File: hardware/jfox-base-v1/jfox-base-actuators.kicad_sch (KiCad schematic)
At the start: 3 parts, among them J80 ACT A, J81 ACT B, J82 ACT C

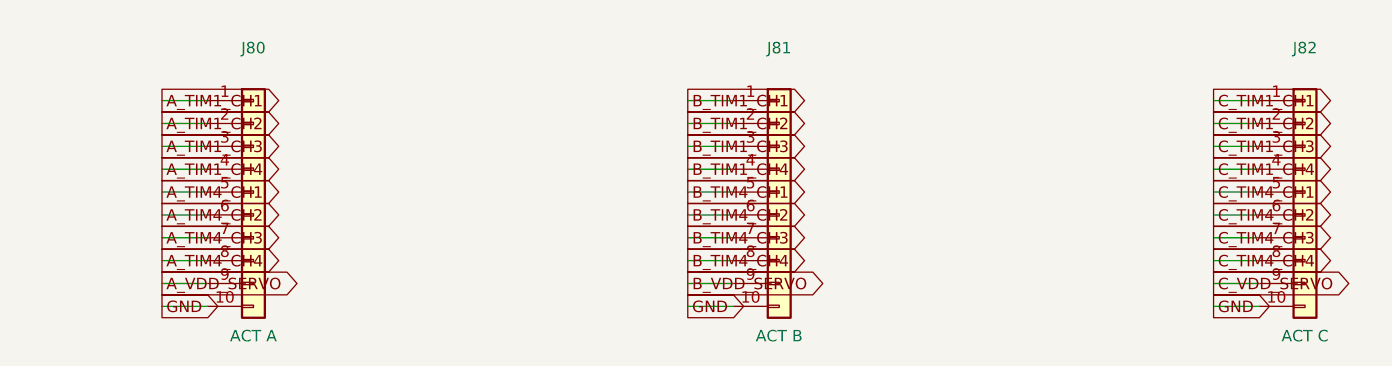
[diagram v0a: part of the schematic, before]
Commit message: LTC4417 lands on the backplane, replacing the diode OR
It left the FCU when the power tree moved and never arrived here - the
backplane has been ORing its two airframe feeds with a pair of Schottkys,
which works and throws away the two things the part was chosen for:

  * Priority. A diode OR takes whichever feed is momentarily higher, so two
    supplies sitting 100 mV apart make the board chatter between them. The
    LTC4417 holds its selection until that source leaves its window.
  * A window. Under- and over-voltage per input, so a feed that has drifted
    out of spec is rejected rather than used because it is the higher of two
    bad ones.

It also drops ~0.4 V across a 5 V rail that the PMOS pass devices do not.

Two inputs, not three. V3 is tied to ground and its pass FET omitted, which
is how the datasheet says to leave an input out; inventing a third feed to
fill it would be worse. D50/D51 stay as reverse-polarity protection.

Three faults surfaced while wiring it, none of them the ORing:

  * The actuator headers still asked each channel for VDD_SERVO. That rail
    left the card's pinout when the power tree moved - servo power now runs
    from the backplane straight to the actuators and never passes through a
    card, which is the right way round. Three nets had nothing driving them.
  * EN was tied to +3V3, a rail the backplane does not have. It regulates
    nothing; the cards do. Now tied to the primary feed, so the part is
    enabled whenever there is power at all.
  * The expansion header overflowed. Its guard reported "25 spare signals
    will not fit a 20-pin header - widen it rather than dropping the
    overflow silently", which is exactly what it was written to catch. 2x15.

The far-face hole check earned itself again: a threshold divider placed on
the back landed under a card socket's through-holes. Bands on the back face
have to thread between sockets at y 20..27, 46..53 and 72..79.

  FCU        DRC 0 blocking, 105 parts, all checks pa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
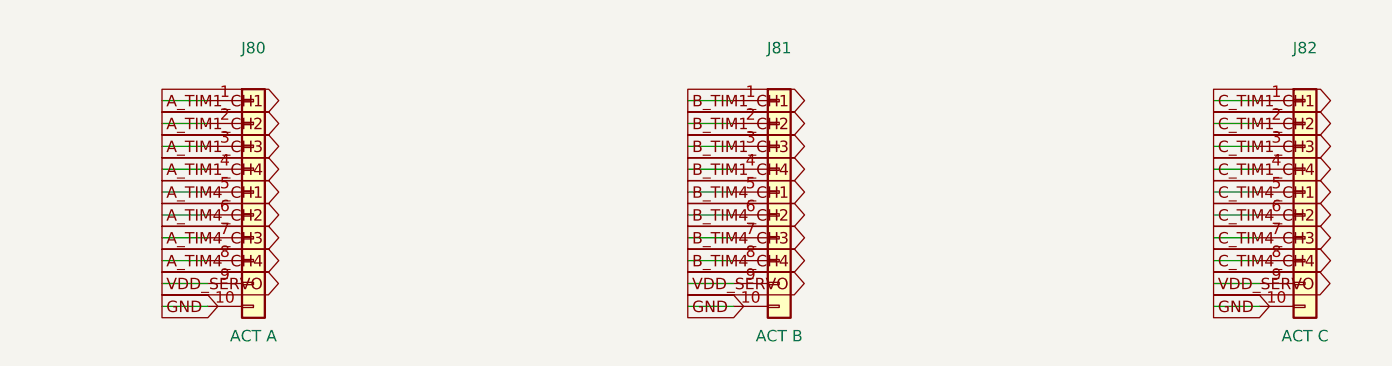
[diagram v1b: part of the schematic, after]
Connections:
- net B_VDD_SERVO is gone; now on net VDD_SERVO: J81.9 (Pin_9)
- net C_VDD_SERVO is gone; now on net VDD_SERVO: J82.9 (Pin_9)
- net A_VDD_SERVO renamed VDD_SERVO
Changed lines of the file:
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@@
 		(instances
 			(project "jfox-base"
-				(path "/ef0cd357-fcbe-4cea-a357-f07c015001bc"
+				(path "/521304b0-d99e-4f3e-bb16-229f8441ae5f"
 					(reference "J80")
 					(unit 1)
@@
 		)
 	)
-	(global_label "A_VDD_SERVO"
+	(global_label "VDD_SERVO"
 		(shape output)
 		(at 57.15 134.62 0)
@@
 		(instances
 			(project "jfox-base"
-				(path "/ef0cd357-fcbe-4cea-a357-f07c015001bc"
+				(path "/521304b0-d99e-4f3e-bb16-229f8441ae5f"
 					(reference "J81")
 					(unit 1)
@@
 		)
 	)
-	(global_label "B_VDD_SERVO"
+	(global_label "VDD_SERVO"
 		(shape output)
 		(at 115.57 134.62 0)
@@
 		(instances
 			(project "jfox-base"
-				(path "/ef0cd357-fcbe-4cea-a357-f07c015001bc"
+				(path "/521304b0-d99e-4f3e-bb16-229f8441ae5f"
 					(reference "J82")
 					(unit 1)
@@
 		)
 	)
-	(global_label "C_VDD_SERVO"
+	(global_label "VDD_SERVO"
 		(shape output)
 		(at 173.99 134.62 0)
